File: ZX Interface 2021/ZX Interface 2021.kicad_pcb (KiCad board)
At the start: 2 copper layers, 87.6 x 99.9 mm, 50 parts, among them J1 AJS #1, J2 AJS #2, J3 SWAP_ROMS, J4 Cartridge, J5 JOYSTICK_EN, M1 Mounting, M2 Mounting, M3 Mounting, M4 Mounting, M5 Mounting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

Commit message: ... and the rest
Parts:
- moved C8 158.3 mm to (160.7, 127.0)
- moved U8 158.3 mm to (164.5, 133.3)
- moved U3 114.2 mm to (109.9, 121.9)
- moved C3 114.2 mm to (106.0, 115.6)
- moved C4 72.6 mm to (106.0, 104.1)
- moved U4 72.6 mm to (109.9, 110.5)
- moved C7 31.9 mm to (160.7, 116.2)
- moved U7 31.9 mm to (164.5, 121.9)
- moved C5 13.7 mm to (104.1, 128.3)
- moved R12 10.2 mm to (155.6, 88.3), turned to 180 degrees
- moved R9 10.2 mm to (132.7, 88.3), turned to 0 degrees
- moved R11 9.69 mm to (186.4, 83.1)
- moved SW1 9.53 mm to (184.2, 76.8), turned to 90 degrees
- moved U6 8.91 mm to (159.4, 110.5)
- moved C6 8.28 mm to (155.6, 104.8)
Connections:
- net /IF2_EN renamed /CARTRIDGE_EN
- J4 pad A17: /~ROM_3 -> /~ROM_OE
- J4 pad A18: /~ROM_2 -> /~ROM_0
- J4 pad A20: /~ROM_0 -> /~ROM_2
- J4 pad A21: /~ROM_OE -> /~ROM_3
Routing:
- net /D3: track 4.71 -> 156.8 mm, vias 0 -> 6
- net /D4: track 9.79 -> 151.9 mm, vias 0 -> 6
- net /D5: track 0.00 -> 135.1 mm, vias 0 -> 8
- net /A11: track 0.00 -> 134.9 mm, vias 0 -> 3
- net /A12: track 0.00 -> 122.8 mm, vias 0 -> 4
- net /D2: track 21.5 -> 141.0 mm, vias 0 -> 5
- net VCC: track 226.3 -> 341.2 mm, vias 0 -> 2
- net /D6: track 0.00 -> 112.4 mm, vias 0 -> 6
- net /D7: track 0.00 -> 111.6 mm, vias 0 -> 6
- net /D1: track 16.3 -> 118.9 mm, vias 0 -> 6
- net /~ROMCS: track 0.00 -> 97.6 mm, vias 0 -> 4
- net /D0: track 28.8 -> 124.1 mm, vias 0 -> 6
- net /~MREQ: track 0.00 -> 91.9 mm, vias 0 -> 5
- net /~IORQ: track 0.00 -> 86.3 mm, vias 0 -> 2
- net /A13: track 0.00 -> 85.7 mm, vias 0 -> 6
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
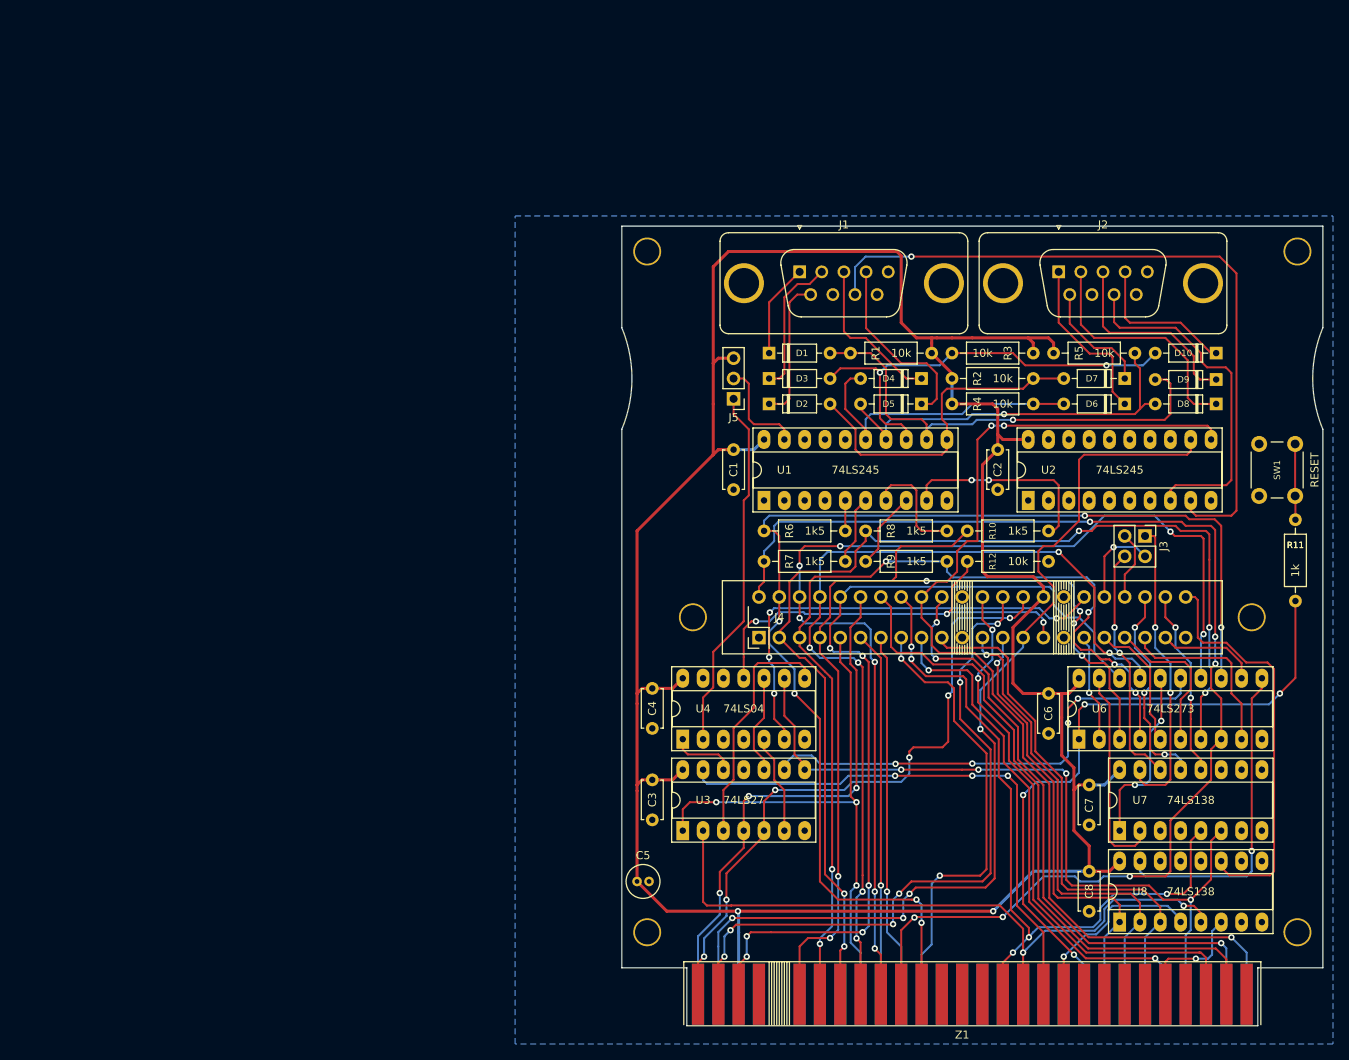
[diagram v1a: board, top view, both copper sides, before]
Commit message: Added some artwork
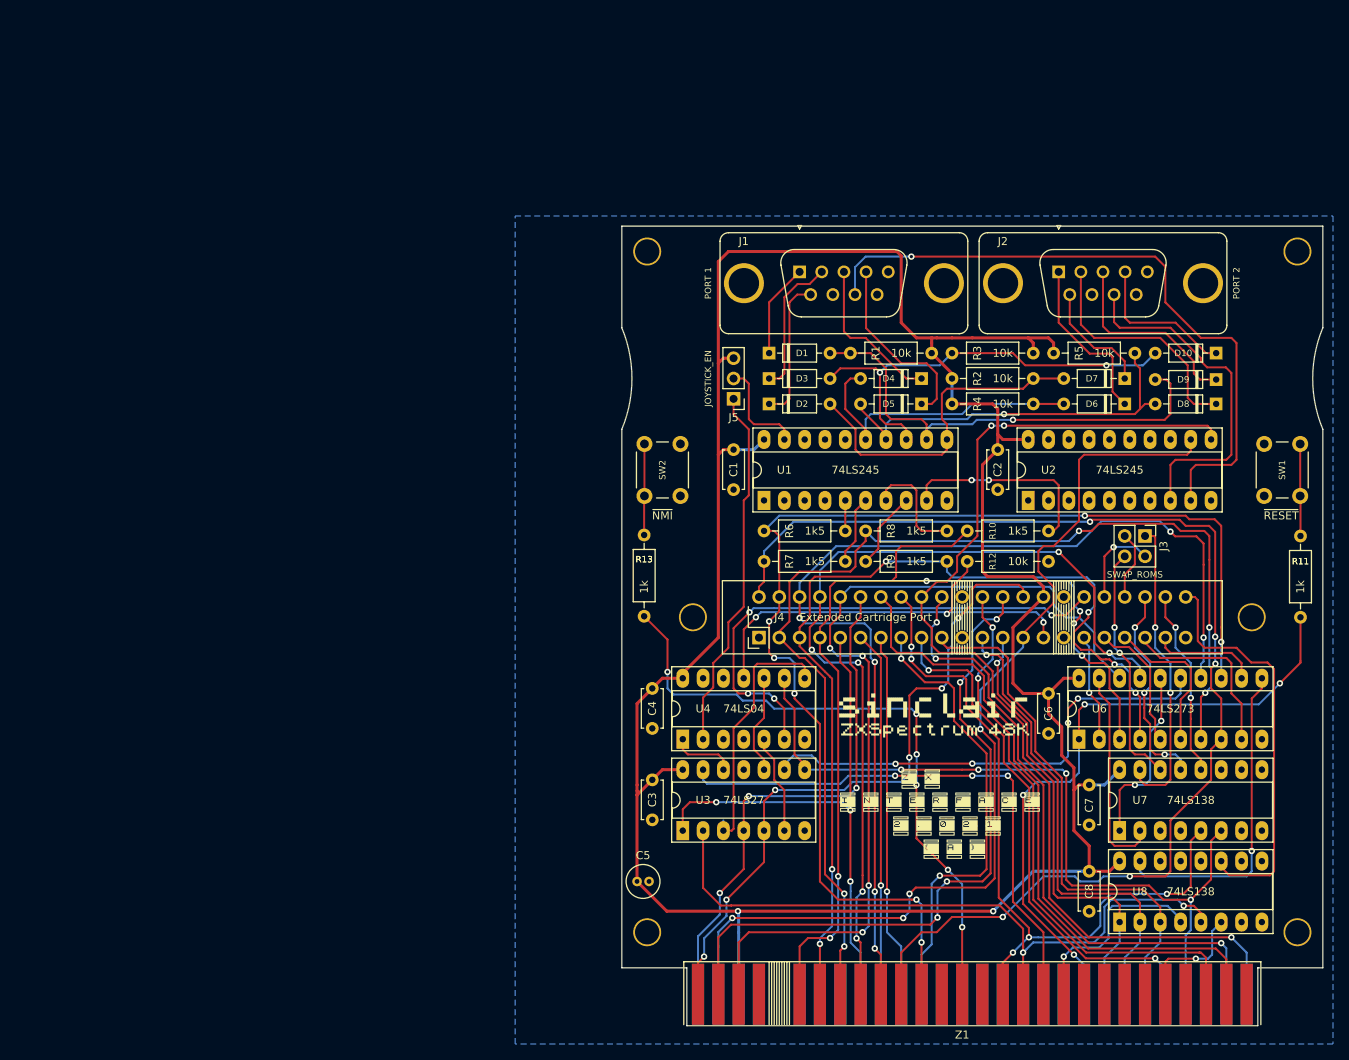
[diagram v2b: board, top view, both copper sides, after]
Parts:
- added R13: 1k, Resistor_THT:R_Axial_DIN0207_L6.3mm_D2.5mm_P10.16mm_Horizontal, F.Cu at (105.0, 85.0)
- added SW2: ~NMI, switch_cutout:SW_PUSH_6mm, F.Cu at (107.3, 76.8)
- added sinclair_title: Val**, artwork:interface_2021, F.Cu at (129.5, 114.3)
- added sinclair_title: , artwork:sinclair_title, F.Cu at (128.9, 104.8)
- J1: value AJS #1 -> PORT 1
- J2: value AJS #2 -> PORT 2
- J4: value Cartridge -> Extended Cartridge Port
- SW1: value RESET -> ~RESET
- moved R11 2.13 mm to (187.1, 85.1)
- moved SW1 0.63 mm to (184.8, 76.8)
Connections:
- Z1 pad A14: (no net) -> /~NMI
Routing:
- net /~NMI: track 0.00 -> 80.1 mm, vias 0 -> 6
- net Net-(R13-Pad1): track 0.00 -> 11.4 mm
- net /~ROM_OE: track 57.9 -> 64.9 mm
- net Net-(J1-Pad8): track 89.7 -> 83.4 mm
- net VCC: track 341.2 -> 336.4 mm
- net /D5: track 135.1 -> 131.8 mm, vias 8 -> 6
- net /D3: track 156.8 -> 154.0 mm, vias 6 -> 5
- net /~RESET: track 84.2 -> 81.7 mm
- net Net-(R11-Pad1): track 9.49 -> 11.5 mm
- net /A15: track 81.3 -> 83.2 mm
- net /~WR: track 23.9 -> 25.1 mm
- net /A0: track 71.0 -> 70.0 mm
- net /D6: track 112.4 -> 111.6 mm
- net /A11: track 134.9 -> 134.2 mm
- net /BA18: track 13.4 -> 14.1 mm
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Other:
- board text added: "ENABLE"
- board text added: "JOYSTICK INTERFACE"
- board text added: "Licensed under CERN OHL v.1.2"
- board text added: "ROM 0"
- board text added: "ROM 1"
- board text added: "SWAP_ROMS"
- board text added: "ZX Interface 2.021"
- board text added: "github.com/tebl"

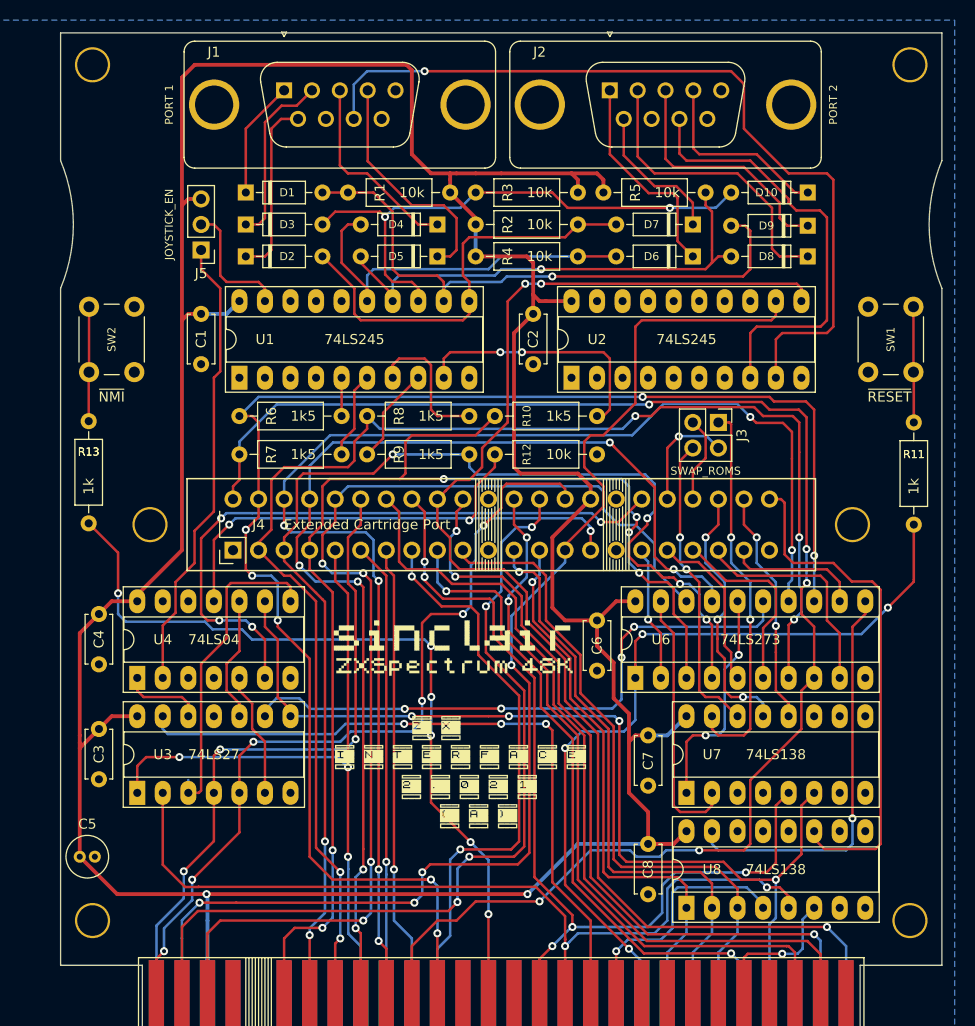
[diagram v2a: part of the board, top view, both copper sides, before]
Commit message: Silkscreen tweaks
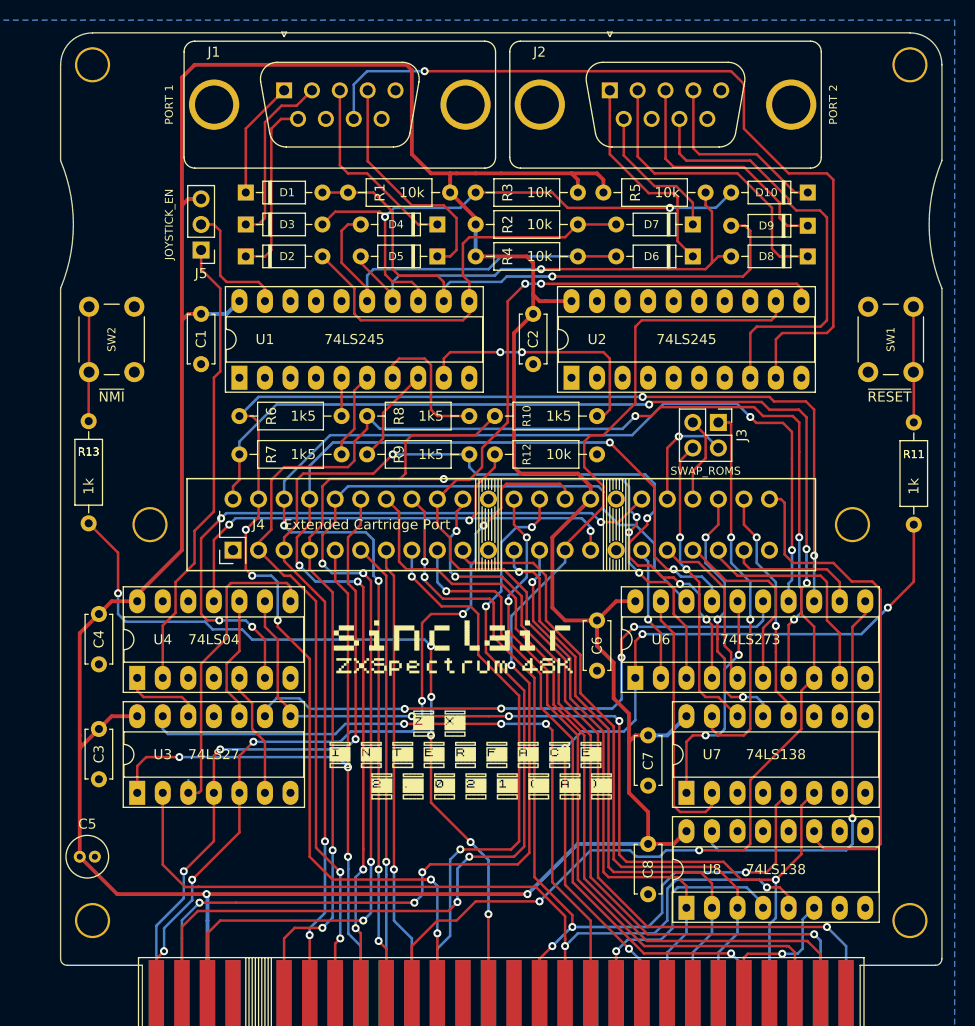
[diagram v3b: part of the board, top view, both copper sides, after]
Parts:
- moved sinclair_title 0.90 mm to (128.9, 113.7)
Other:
- outline, holes or cut-outs redrawn
- board text added: "ATARI PORT 1"
- board text added: "ATARI PORT 2"
- board text added: "SLOT"
- board text added: "USE ONLY WITH ATARI DB9 RANGE OF JOYSTICKS"
